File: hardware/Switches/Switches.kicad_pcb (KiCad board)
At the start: 4 copper layers, 120 x 75 mm, 108 parts, among them J101 BusBar, J102 BusBar, J103 BusBar, J104 BusBar, J105 Conn_02x03_Odd_Even, Q101 IPT015N10N5, Q102 IPT015N10N5, Q103 IPT015N10N5, Q104 IPT015N10N5, Q105 IPT015N10N5, Q106 IPT015N10N5, Q107 IPT015N10N5, Q108 IPT015N10N5, Q109 IPT015N10N5, Q110 IPT015N10N5, Q111 IPT015N10N5, Q112 IPT015N10N5, U101 UCC27211DDAR, U102 UCC27211DDAR

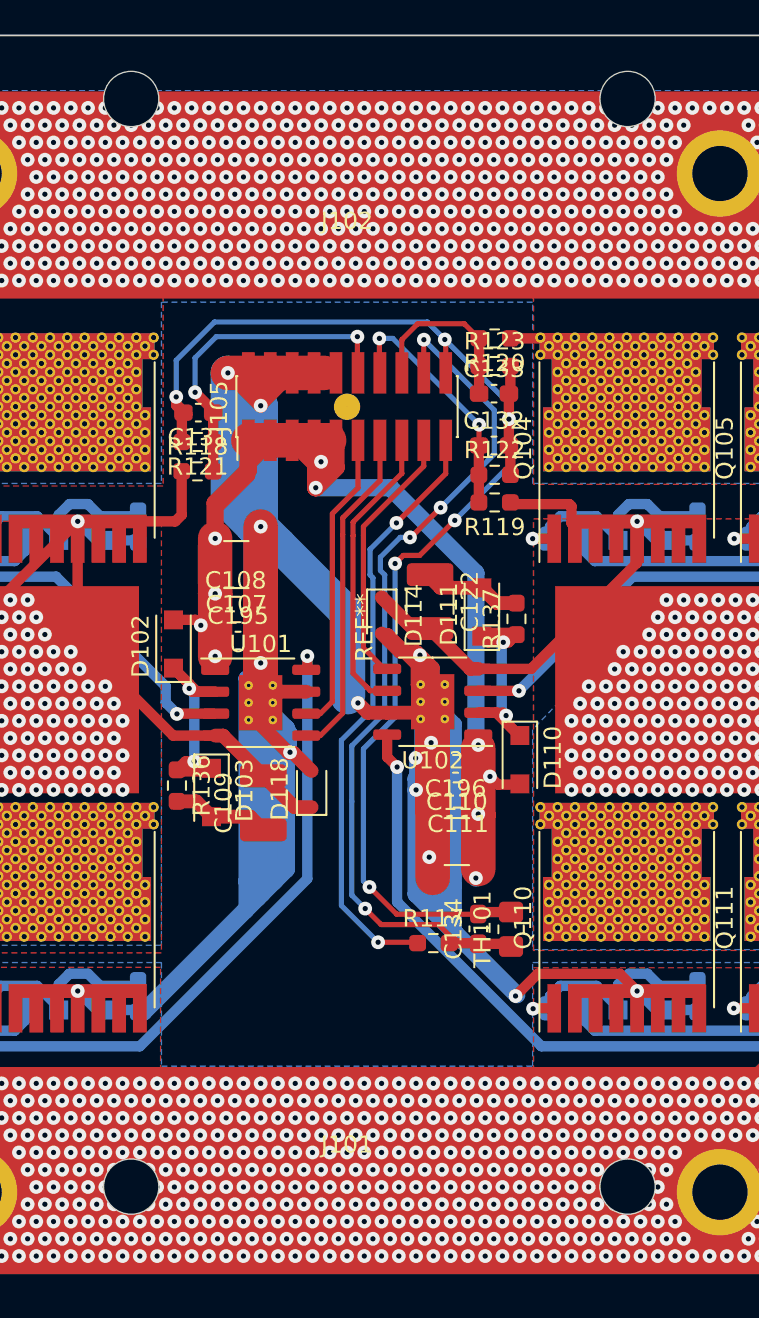
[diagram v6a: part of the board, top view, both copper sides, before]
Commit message: A lot of clarance issues fixed, gerbers added
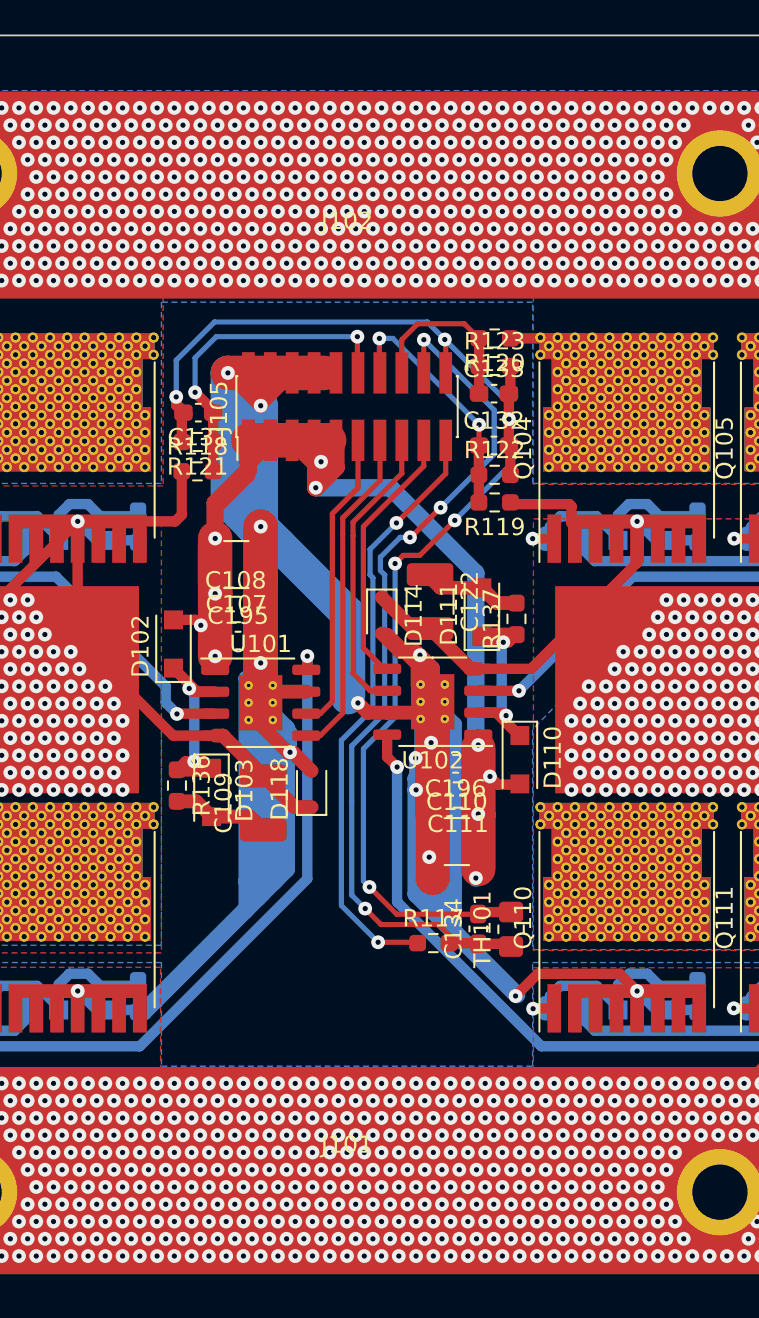
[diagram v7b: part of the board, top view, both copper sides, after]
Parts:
- removed REF**: ControleHoles, Switches:ControleHoles
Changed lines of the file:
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@@
     (tracks 4009)
     (zones 0)
-    (modules 108)
+    (modules 107)
     (nets 40)
   )
   (page A4)
   (layers
-    (0 F.Cu mixed hide)
-    (1 In1.Cu mixed hide)
-    (2 In2.Cu mixed hide)
-    (31 B.Cu mixed hide)
-    (32 B.Adhes user hide)
-    (33 F.Adhes user hide)
+    (0 F.Cu mixed)
+    (1 In1.Cu mixed)
+    (2 In2.Cu mixed)
+    (31 B.Cu mixed)
+    (32 B.Adhes user)
+    (33 F.Adhes user)
     (34 B.Paste user hide)
     (35 F.Paste user hide)
@@
     (pcbplotparams
       (layerselection 0x010fc_ffffffff)
-      (usegerberextensions false)
-      (usegerberattributes true)
-      (usegerberadvancedattributes true)
+      (usegerberextensions true)
+      (usegerberattributes false)
+      (usegerberadvancedattributes false)
       (creategerberjobfile true)
       (excludeedgelayer true)
@@
       (plotinvisibletext false)
       (padsonsilk false)
-      (subtractmaskfromsilk false)
+      (subtractmaskfromsilk true)
       (outputformat 1)
       (mirror false)
@@
     (add_net "Net-(R114-Pad2)")
   )
-  (module Switches:ControleHoles (layer F.Cu)
-    (at 162.75 97.85 90)
-    (fp_text reference REF** (at 0 0.5 90) (layer F.SilkS)
-      (effects (font (size 1 1) (thickness 0.15)))
-    )
-    (fp_text value ControleHoles (at 0 -0.5 90) (layer F.Fab)
-      (effects (font (size 1 1) (thickness 0.15)))
-    )
-    (pad "" np_thru_hole circle (at -32.37842 -12.99954 90) (size 3.200001 3.200001) (drill 3.200001) (layers *.Cu *.Mask))
-    (pad "" np_thru_hole circle (at 30.61758 -12.99954 90) (size 3.200001 3.200001) (drill 3.200001) (layers *.Cu *.Mask))
-    (pad "" np_thru_hole circle (at -32.37842 15.75046 90) (size 3.200001 3.200001) (drill 3.200001) (layers *.Cu *.Mask))
-    (pad "" np_thru_hole circle (at 30.61758 15.75046 90) (size 3.200001 3.200001) (drill 3.200001) (layers *.Cu *.Mask))
-    (pad "" thru_hole circle (at 12.79144 -0.49784 90) (size 1.524 1.524) (drill 0.0254) (layers *.Cu *.Mask))
-  )
   (module Switches:Infineon_PG-HSOF-8-1_ThermalVias3 locked (layer F.Cu)

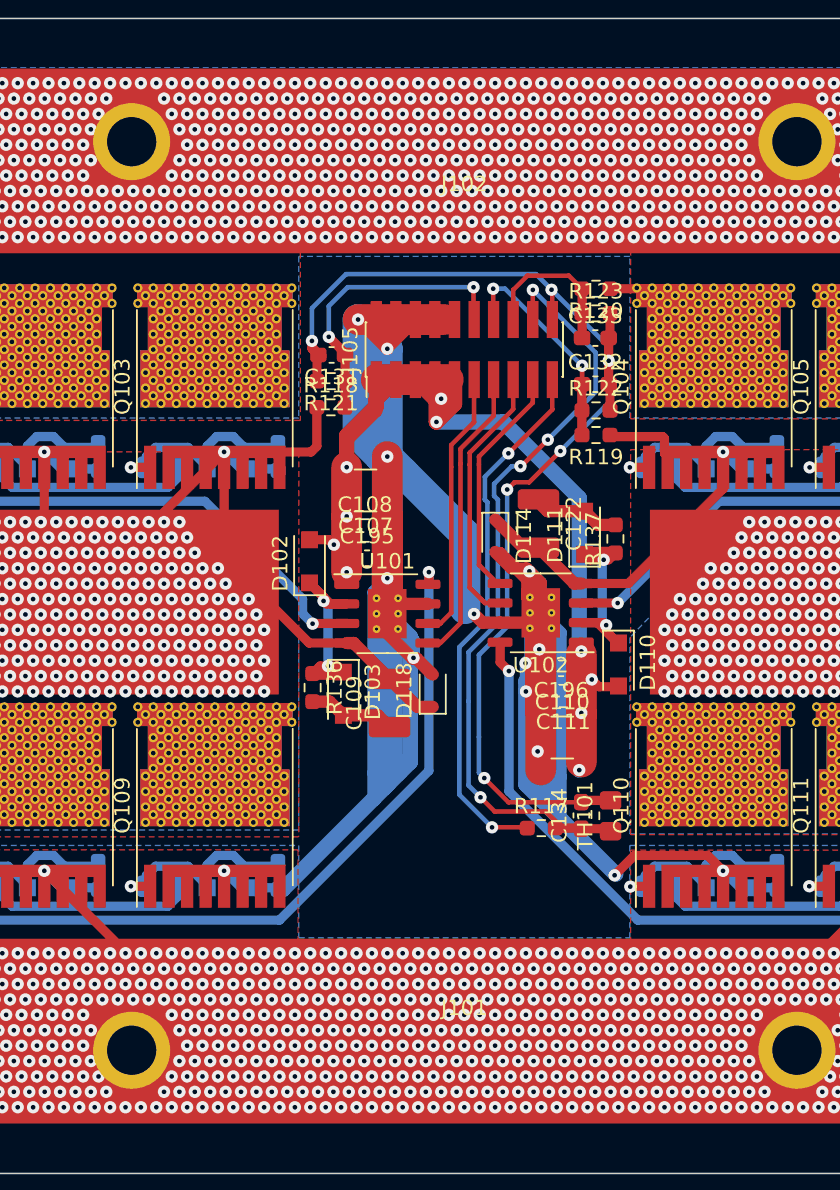
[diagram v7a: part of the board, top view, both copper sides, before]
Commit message: PCB updated with holes
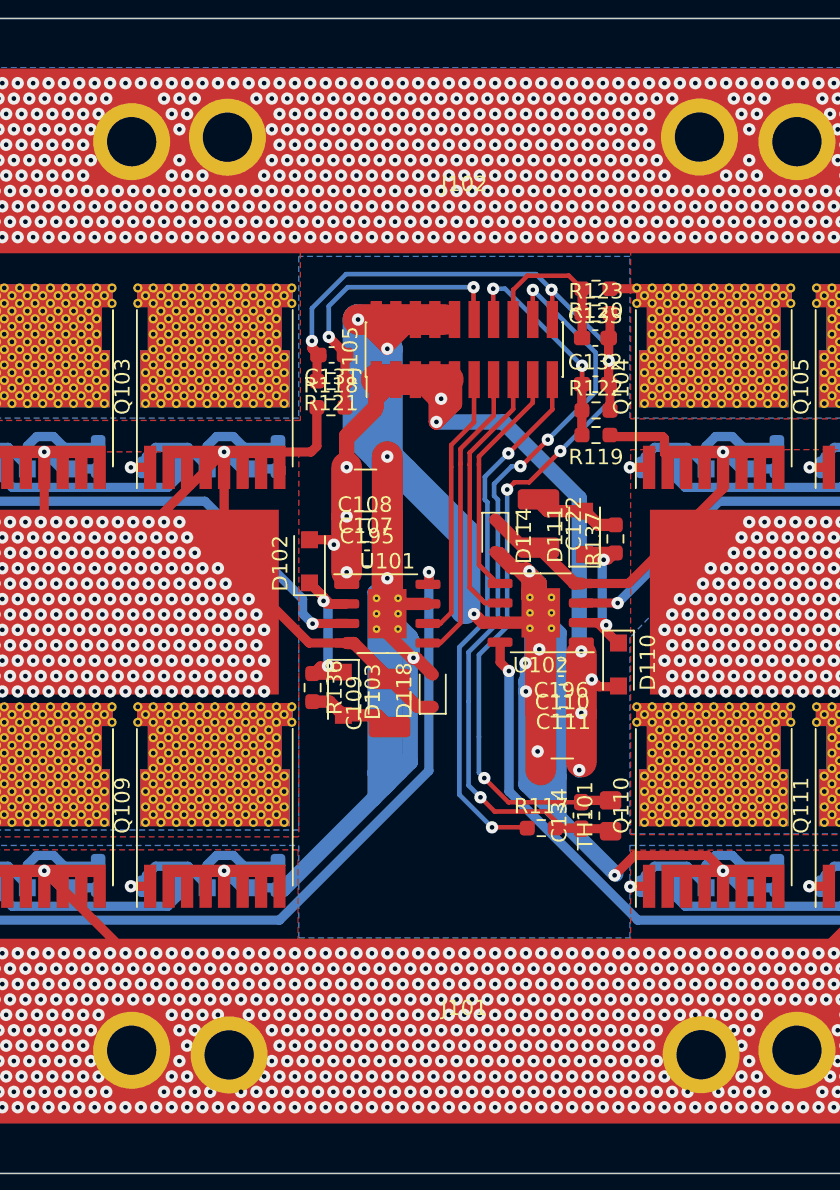
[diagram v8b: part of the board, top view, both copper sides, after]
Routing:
- net GND: vias 1106 -> 1067
- net +BATT: vias 1088 -> 1033
- net (no net): vias 0 -> 1
